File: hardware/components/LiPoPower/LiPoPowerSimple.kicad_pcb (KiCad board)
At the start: 2 copper layers, 38 parts, among them J101 Battery, J102 Ext Switch, J103 LiPo, SW101 Power Switch, U101 MCP73871-1CC, U102 TPS63070RNMR, U103 INA226

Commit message: 各コンポーネントの修正をしました．一度プッシュします(多分コンフリクトするので)．
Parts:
- J102: footprint Connector_JST:JST_PH_S2B-PH-K_1x02_P2.00mm_Horizontal -> Connector_JST:JST_XH_S2B-XH-A_1x02_P2.50mm_Horizontal
- LED101, LED102, LED103: footprint LED_SMD:LED_0603_1608Metric -> LED_SMD:LED_0805_2012Metric
- R101, R102, R104, R105, R106, R108, R111: footprint PCM_Resistor_SMD_AKL:R_0402_1005Metric -> Resistor_SMD:R_0402_1005Metric
- R103: value 47k -> 100k; footprint PCM_Resistor_SMD_AKL:R_0402_1005Metric -> Resistor_SMD:R_0402_1005Metric
- R109: value 150k -> 15k; footprint PCM_Resistor_SMD_AKL:R_0402_1005Metric -> Resistor_SMD:R_0402_1005Metric
- R110: value 470k -> 47k; footprint PCM_Resistor_SMD_AKL:R_0402_1005Metric -> Resistor_SMD:R_0402_1005Metric
- RV101: value 20k -> 10k; footprint PCM_Potentiometer_SMD_AKL:Potentiometer_Bourns_TC33X_Vertical -> Potentiometer_SMD:Potentiometer_Bourns_TC33X_Vertical
- SW101: footprint Button_Switch_THT:SW_CuK_OS102011MA1QN1_SPDT_Angled -> Button_Switch_THT:SW_Slide_SPDT_Angled_CK_OS102011MA1Q
- moved F101 32.2 mm to (134.0, 83.5), turned to 90 degrees
- moved LED101 28.9 mm to (136.2, 83.9), turned to 90 degrees
- moved R101 26.7 mm to (138.2, 84.8)
- moved LED103 2.34 mm to (166.6, 71.8)
- moved J102 1.55 mm to (162.6, 72.1)
- moved R104 1.15 mm to (158.0, 75.5)
- moved R106 1.15 mm to (160.1, 75.5)
- moved R111 1.15 mm to (162.1, 75.5)
- moved C106 0.99 mm to (146.0, 75.9)
- moved LED102 0.24 mm to (153.5, 71.7)
- moved R102 0.11 mm to (147.4, 81.5), turned to -90 degrees
- turned RV101 to 180 degrees
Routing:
- net GND: track 19.8 -> 91.5 mm, vias 0 -> 10
- net Net-(D101-K): track 6.68 -> 52.4 mm, vias 0 -> 4
- net Net-(J102-Pin_2): track 0.00 -> 44.5 mm, vias 0 -> 2
- net Net-(J102-Pin_1): track 0.00 -> 33.2 mm, vias 0 -> 1
- net Net-(U101-V_{BAT_SENSE}): track 0.00 -> 23.1 mm
- net VDD: track 8.58 -> 27.0 mm, vias 0 -> 2
- net Net-(LED101-A): track 0.00 -> 11.6 mm, vias 0 -> 2
- net /I2C_SCL: track 0.00 -> 11.0 mm, vias 0 -> 2
- net Net-(U103-Vbus): track 0.00 -> 11.0 mm, vias 0 -> 2
- net /I2C_SDA: track 0.00 -> 9.87 mm, vias 0 -> 1
- net Net-(U101-CE): track 0.00 -> 8.45 mm, vias 0 -> 2
- net Net-(LED103-K): track 0.00 -> 5.37 mm
- net Net-(U102-FB): track 0.00 -> 4.66 mm
- net Net-(U102-VAUX): track 0.00 -> 4.49 mm
- net Net-(U102-PG): track 0.00 -> 4.44 mm
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
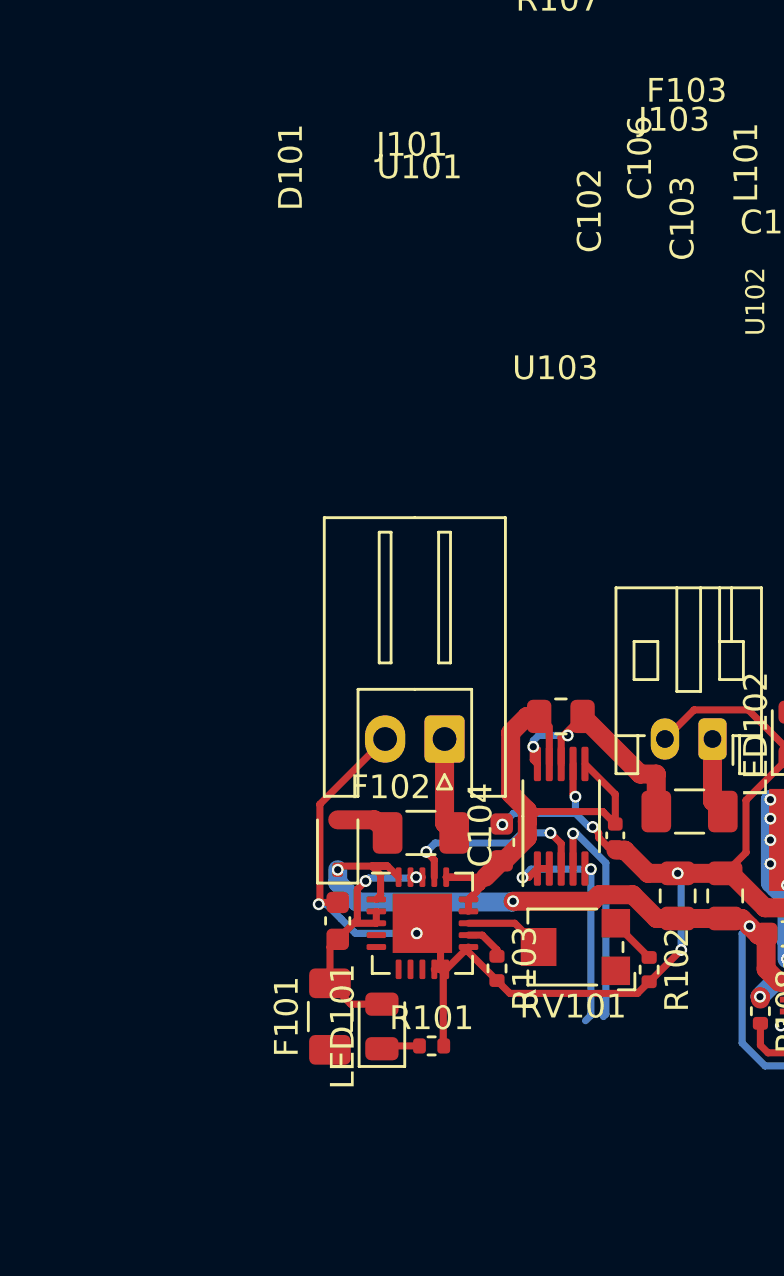
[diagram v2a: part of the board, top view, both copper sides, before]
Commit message: Mission基板のオーダーファイルの作成・コンポーネント修正（LiPoバックアップ切り替え、GNSS書き込み、usbプルダウン抵抗）
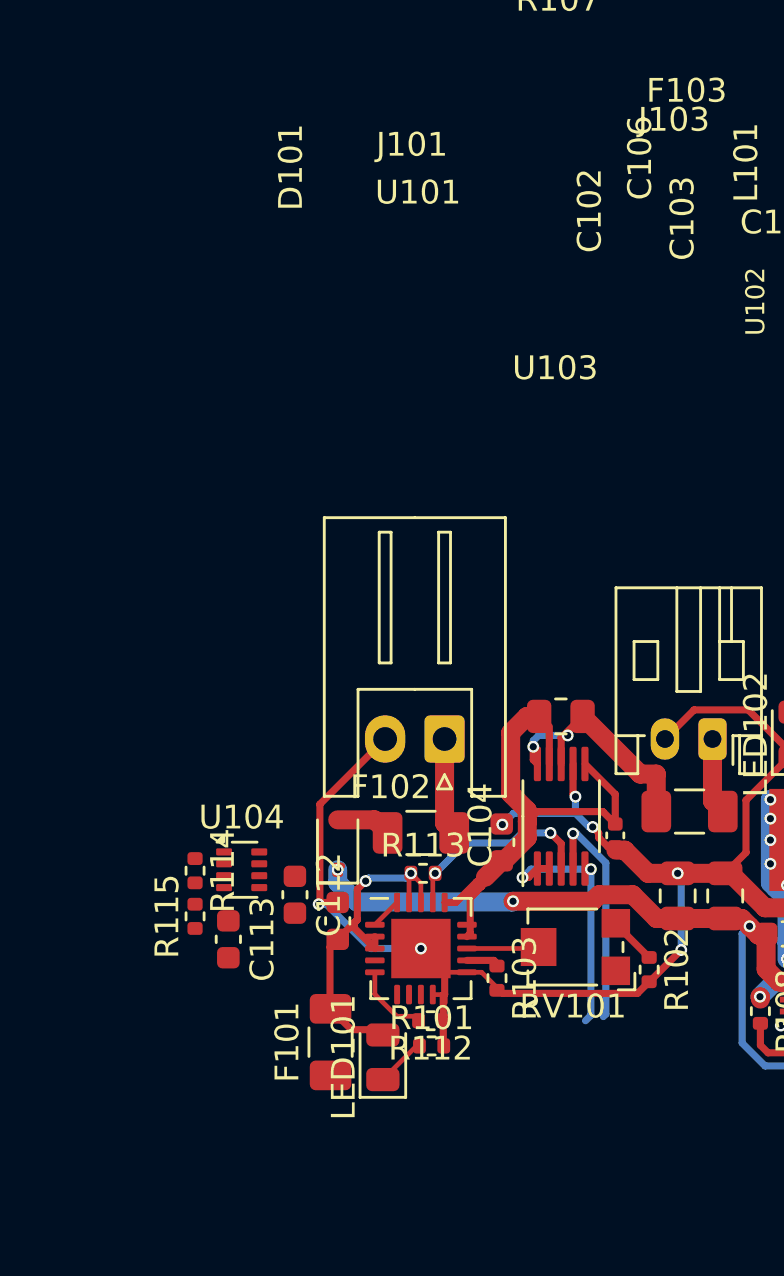
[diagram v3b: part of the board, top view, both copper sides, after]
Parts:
- added C112: 10uF, Capacitor_SMD:C_0603_1608Metric, F.Cu at (132.5, 78.4)
- added C113: 10uF, Capacitor_SMD:C_0603_1608Metric, F.Cu at (129.7, 80.3)
- added R112: 10k, Resistor_SMD:R_0402_1005Metric, F.Cu at (138.2, 83.7)
- added R113: 100k, Resistor_SMD:R_0402_1005Metric, F.Cu at (137.9, 77.5)
- added R114: 4.7k, Resistor_SMD:R_0402_1005Metric, F.Cu at (128.3, 77.4)
- added R115: 10k, Resistor_SMD:R_0402_1005Metric, F.Cu at (128.3, 79.3)
- added U104: TPS2116DRL, Package_TO_SOT_SMD:SOT-583-8, F.Cu at (130.3, 77.3)
- moved LED101 1.30 mm to (136.2, 85.2)
- moved F101 1.08 mm to (134.0, 84.6)
- moved U101 1.06 mm to (137.8, 80.7)
- moved R103 0.41 mm to (141.0, 81.9)
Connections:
- C102 pad 1: Net-(D101-K) -> Net-(U102-VIN)
- C103 pad 1: Net-(D101-K) -> Net-(U102-VIN)
- C105 pad 1: Net-(D101-K) -> Net-(U102-VIN)
- R104 pad 1: Net-(D101-K) -> Net-(U102-VIN)
- U101 pad 1: Net-(D101-K) -> Net-(U104-MODE)
- U101 pad 20: Net-(D101-K) -> Net-(U104-MODE)
- U101 pad 5: unconnected-(U101-THERM-Pad5) -> Net-(U101-THERM)
- U102 pad 12_13: Net-(D101-K) -> Net-(U102-VIN)
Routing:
- net Net-(D101-K): track 52.4 -> 47.5 mm
- net Net-(LED101-A): track 11.6 -> 15.5 mm
- net Net-(U101-THERM): track 0.00 -> 3.22 mm
- net GND: track 91.5 -> 93.6 mm
- net Net-(U104-MODE): track 0.00 -> 1.33 mm

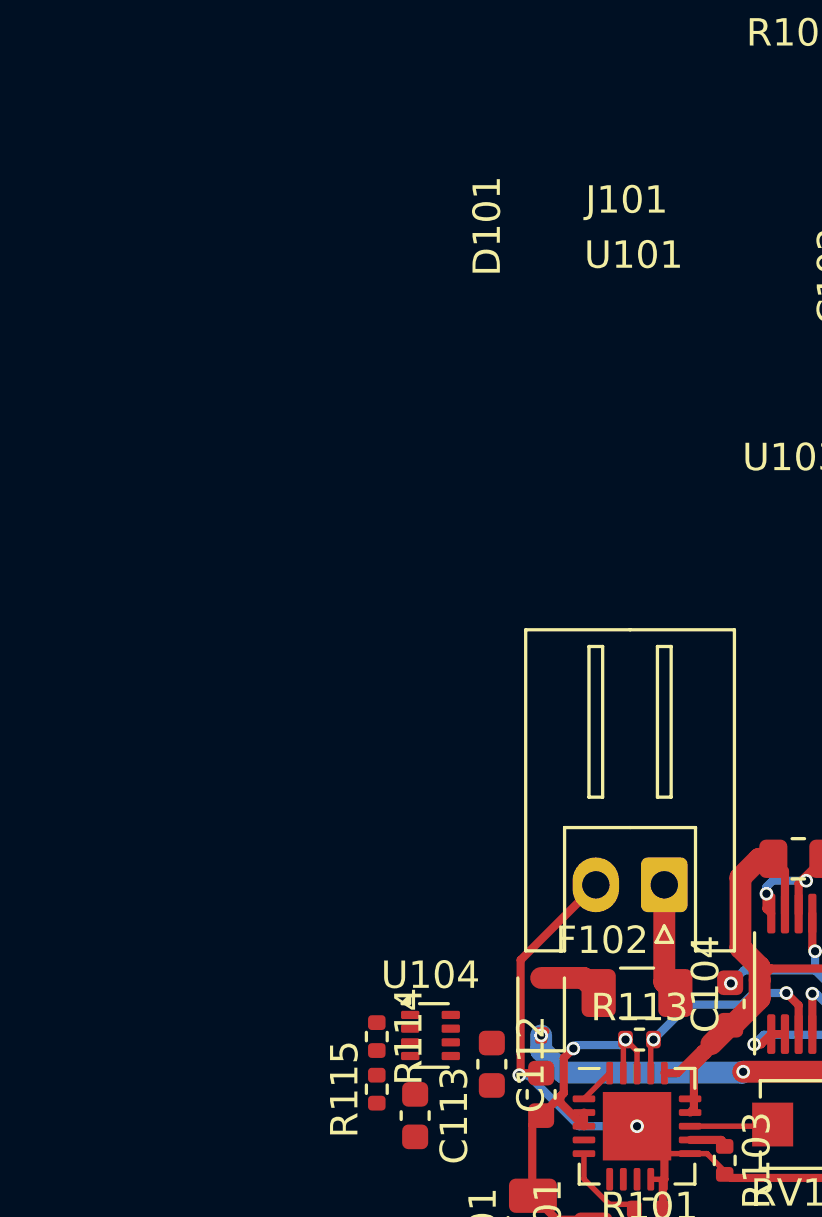
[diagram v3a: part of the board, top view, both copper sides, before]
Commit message: 電源回路を修正しました。 ヒーターのダミーロードはどうするか思いつかなかったので、そのままにしています。
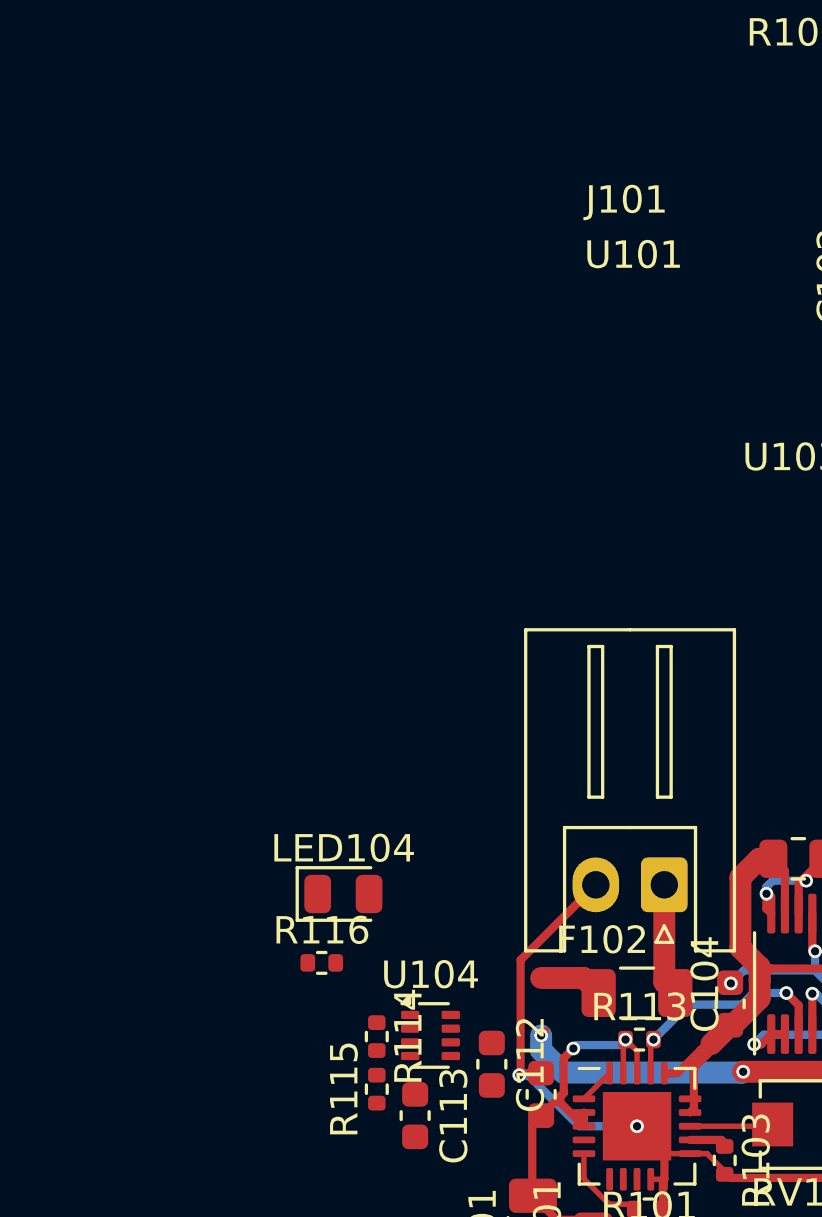
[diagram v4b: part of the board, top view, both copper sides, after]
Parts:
- removed D101: D_Schottky, Diode_SMD:D_SOD-323
- added LED104: Backup, LED_SMD:LED_0805_2012Metric, F.Cu at (127.1, 72.2)
- added R116: 1k, Resistor_SMD:R_0402_1005Metric, F.Cu at (126.3, 74.7)
- R114: value 4.7k -> 47k
- R115: value 10k -> 100k
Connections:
- C102 pad 1: Net-(U102-VIN) -> Net-(LED104-A)
- C103 pad 1: Net-(U102-VIN) -> Net-(LED104-A)
- C105 pad 1: Net-(U102-VIN) -> Net-(LED104-A)
- C106 pad 1: Net-(U101-V_{BAT_SENSE}) -> Net-(LED104-A)
- C112 pad 1: Net-(D101-K) -> Net-(U104-VIN2)
- F102 pad 2: Net-(D101-A) -> Net-(U104-VIN2)
- R104 pad 1: Net-(U102-VIN) -> Net-(LED104-A)
- U102 pad 12_13: Net-(U102-VIN) -> Net-(LED104-A)
- U103 pad 6: Net-(U101-V_{BAT_SENSE}) -> Net-(LED104-A)
- U104 pad 2: Net-(U102-VIN) -> Net-(LED104-A)
- U104 pad 6: Net-(D101-K) -> Net-(U104-VIN2)
- U104 pad 7: Net-(U102-VIN) -> Net-(LED104-A)
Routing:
- net Net-(LED104-A): track 0.00 -> 47.5 mm, vias 0 -> 4
- net Net-(D101-K): track 47.5 -> 0.00 mm, vias 4 -> 0
- net Net-(U104-VIN2): track 0.00 -> 2.33 mm
- net Net-(D101-A): track 2.33 -> 0.00 mm
